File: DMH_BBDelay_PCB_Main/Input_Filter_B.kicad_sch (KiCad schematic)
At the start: 15 parts, among them U21 TL072

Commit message: Adjustments during breadboarding
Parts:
- removed C112: 4.7uF, Capacitor_THT:CP_Radial_D4.0mm_P1.50mm, symbol Device:C_Polarized
- removed R106, R243: 22k, Resistor_THT:R_Axial_DIN0207_L6.3mm_D2.5mm_P7.62mm_Horizontal, symbol Device:R_US
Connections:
- net Ref_2v5: now reaches U21.5 (+)

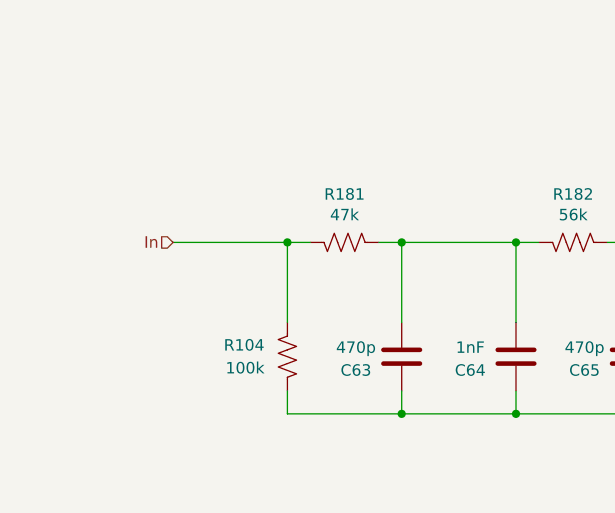
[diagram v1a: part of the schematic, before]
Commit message: More adjustments during breadboarding
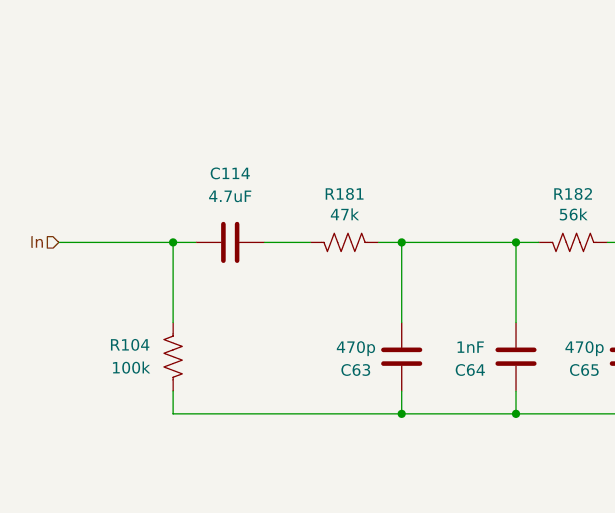
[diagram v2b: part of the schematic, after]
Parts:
- added C114: 4.7uF, Capacitor_THT:C_Disc_D4.3mm_W1.9mm_P5.00mm, symbol Device:C
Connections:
- net In: now also C114.1; no longer R181.1
- new net: C114.2, R181.1
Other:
- moved on the sheet: R104
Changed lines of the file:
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@@
+	)
+	(junction
+		(at 38.1 63.5)
+		(diameter 0)
+		(color 0 0 0 0)
 	)
 	(junction
@@
 	)
 	(junction
-		(at 50.8 63.5)
+		(at 101.6 82.55)
 		(diameter 0)
 		(color 0 0 0 0)
@@
 	)
 	(junction
-		(at 101.6 82.55)
-		(diameter 0)
-		(color 0 0 0 0)
-	)
-	(junction
 		(at 101.6 63.5)
 		(diameter 0)
@@
 	(wire
 		(pts
-			(xy 50.8 80.01) (xy 50.8 82.55)
+			(xy 38.1 80.01) (xy 38.1 82.55)
 		)
 		(stroke
@@
 	(wire
 		(pts
-			(xy 50.8 63.5) (xy 53.34 63.5)
-		)
-		(stroke
-			(width 0)
-			(type default)
-		)
-	)
-	(wire
-		(pts
 			(xy 86.36 63.5) (xy 88.9 63.5)
 		)
@@
 	(wire
 		(pts
-			(xy 50.8 82.55) (xy 63.5 82.55)
+			(xy 38.1 82.55) (xy 63.5 82.55)
 		)
 		(stroke
@@
 	(wire
 		(pts
+			(xy 38.1 63.5) (xy 40.64 63.5)
+		)
+		(stroke
+			(width 0)
+			(type default)
+		)
+	)
+	(wire
+		(pts
 			(xy 76.2 80.01) (xy 76.2 82.55)
 		)
@@
 	(wire
 		(pts
-			(xy 38.1 63.5) (xy 50.8 63.5)
+			(xy 25.4 63.5) (xy 38.1 63.5)
 		)
 		(stroke
@@
 	(wire
 		(pts
-			(xy 50.8 63.5) (xy 50.8 72.39)
+			(xy 38.1 63.5) (xy 38.1 72.39)
 		)
 		(stroke
@@
 		(pts
 			(xy 123.19 50.8) (xy 114.3 50.8)
+		)
+		(stroke
+			(width 0)
+			(type default)
+		)
+	)
+	(wire
+		(pts
+			(xy 48.26 63.5) (xy 53.34 63.5)
 		)
 		(stroke
@@
 	(hierarchical_label "In"
 		(shape input)
-		(at 38.1 63.5 180)
+		(at 25.4 63.5 180)
 		(effects
 			(font
@@
 	)
 	(symbol
+		(lib_id "Device:C")
+		(at 44.45 63.5 90)
+		(unit 1)
+		(body_style 1)
+		(exclude_from_sim no)
+		(in_bom yes)
+		(on_board yes)
+		(in_pos_files yes)
+		(dnp no)
+		(fields_autoplaced yes)
+		(property "Reference" "C114"
+			(at 44.45 55.88 90)
+			(show_name no)
+			(do_not_autoplace no)
+			(effects
+				(font
+					(size 1.27 1.27)
+				)
+			)
+		)
+		(property "Value" "4.7uF"
+			(at 44.45 58.42 90)
+			(show_name no)
+			(do_not_autoplace no)
+			(effects
+				(font
+					(size 1.27 1.27)
+				)
+			)
+		)
+		(property "Footprint" "Capacitor_THT:C_Disc_D4.3mm_W1.9mm_P5.00mm"
+			(at 48.26 62.5348 0)
+			(hide yes)
+			(show_name no)
+			(do_not_autoplace no)
+			(effects
+				(font
+					(size 1.27 1.27)
+				)
+			)
+		)
+		(property "Datasheet" ""
+			(at 44.45 63.5 0)
+			(hide yes)
+			(show_name no)
+			(do_not_autoplace no)
+			(effects
+				(font
+					(size 1.27 1.27)
+				)
+			)
+		)
+		(property "Description" "Unpolarized capacitor"
+			(at 44.45 63.5 0)
+			(hide yes)
+			(show_name no)
+			(do_not_autoplace no)
+			(effects
+				(font
+					(size 1.27 1.27)
+				)
+			)
+		)
+		(pin "1"
+		)
+		(pin "2"
+		)
+		(instances
+			(project "DMH_BBDelay_PCB_Main"
+				(path "/58f4306d-5387-4983-bb08-41a2313fd315/53120047-129a-4e0f-876f-6cafa2f18733/9104bdbd-0802-4c59-bf61-2977ca5bff15"
+					(reference "C114")
+					(unit 1)
+				)
+			)
+		)
+	)
+	(symbol
 		(lib_id "Device:R_US")
 		(at 107.95 63.5 90)
@@
 	(symbol
 		(lib_id "Device:R_US")
-		(at 50.8 76.2 0)
+		(at 38.1 76.2 0)
 		(mirror x)
 		(unit 1)
@@
 		(dnp no)
 		(property "Reference" "R104"
-			(at 48.26 74.9299 0)
+			(at 35.56 74.9299 0)
 			(show_name no)
 			(do_not_autoplace no)
@@
 		)
 		(property "Value" "100k"
-			(at 48.26 77.4699 0)
+			(at 35.56 77.4699 0)
 			(show_name no)
 			(do_not_autoplace no)
@@
 		)
 		(property "Footprint" "Resistor_THT:R_Axial_DIN0207_L6.3mm_D2.5mm_P7.62mm_Horizontal"
-			(at 51.816 75.946 90)
+			(at 39.116 75.946 90)
 			(hide yes)
 			(show_name no)
@@
 		)
 		(property "Datasheet" ""
-			(at 50.8 76.2 0)
+			(at 38.1 76.2 0)
 			(hide yes)
 			(show_name no)
@@
 		)
 		(property "Description" "Resistor, US symbol"
-			(at 50.8 76.2 0)
-			(hide yes)
-			(show_name no)
+			(at 38.1 76.2 0)
+			(hide yes)
+			(show_name no)

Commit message: Added notes from troubleshooting
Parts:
- C114: value 4.7uF -> 3.3uF
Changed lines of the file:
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@@
 			)
 		)
-		(property "Value" "4.7uF"
+		(property "Value" "3.3uF"
 			(at 44.45 58.42 90)
 			(show_name no)

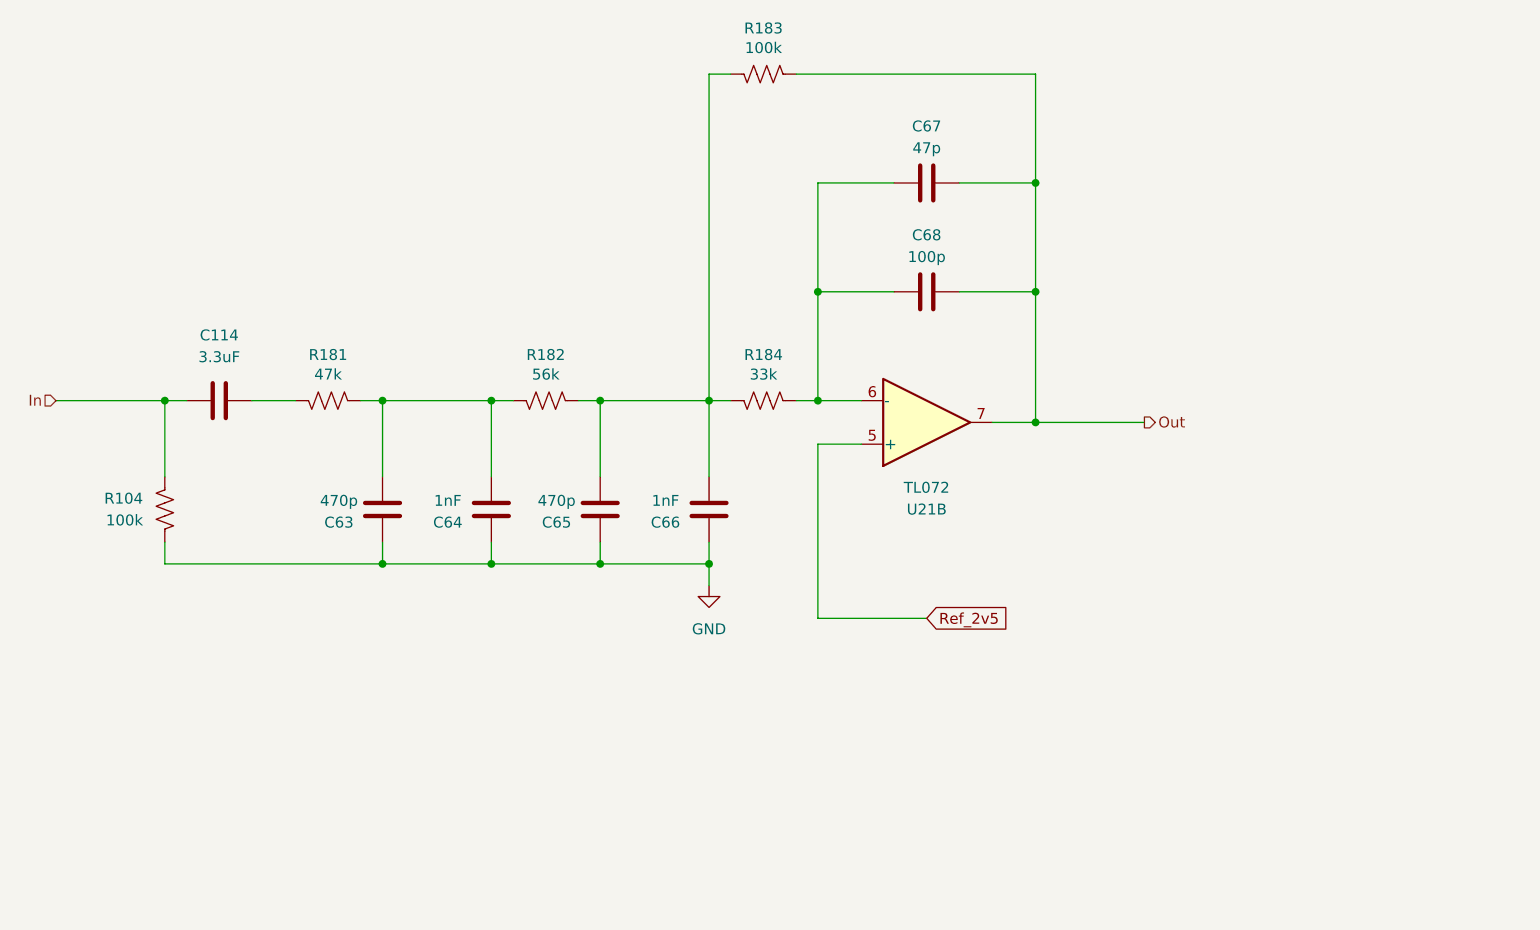
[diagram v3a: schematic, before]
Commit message: Synced channel A and B schematics
... and applied several minor improvements and optimizations.
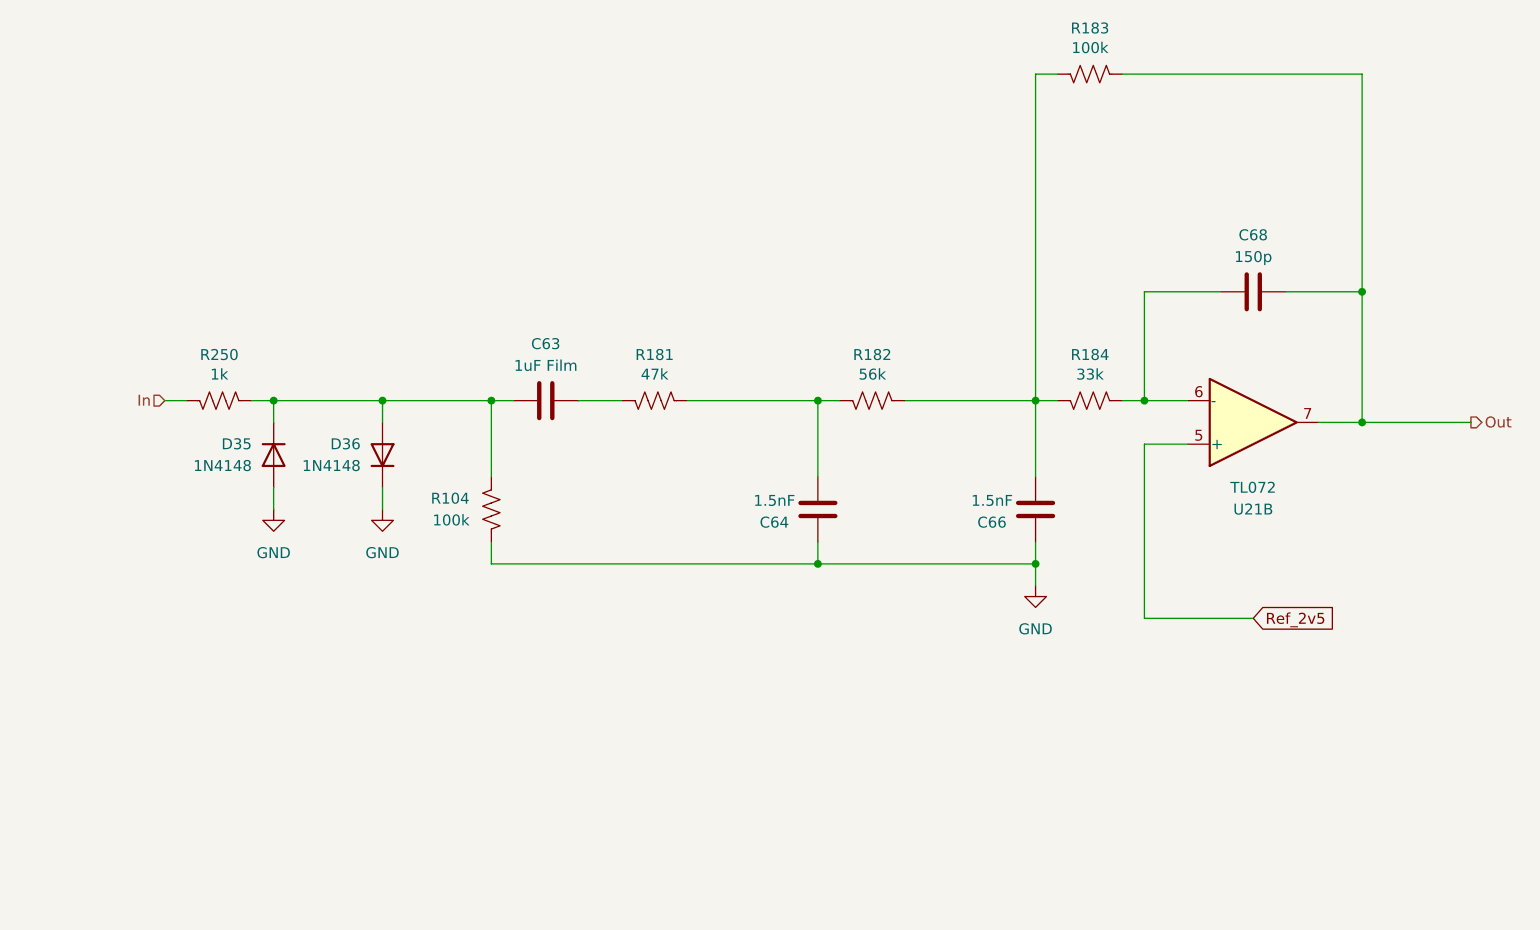
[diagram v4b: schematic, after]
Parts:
- removed C114: 3.3uF, Capacitor_THT:C_Disc_D4.3mm_W1.9mm_P5.00mm, symbol Device:C
- removed C65: 470p, Capacitor_THT:C_Disc_D3.0mm_W2.0mm_P2.50mm, symbol Device:C
- removed C67: 47p, Capacitor_THT:C_Disc_D3.0mm_W2.0mm_P2.50mm, symbol Device:C
- added D35, D36: 1N4148, Diode_THT:D_DO-35_SOD27_P7.62mm_Horizontal, symbol Diode:1N4148
- added R250: 1k, Resistor_THT:R_Axial_DIN0207_L6.3mm_D2.5mm_P7.62mm_Horizontal, symbol Device:R_US
- C63: value 470p -> 1uF Film; footprint Capacitor_THT:C_Disc_D3.0mm_W2.0mm_P2.50mm -> Capacitor_THT:C_Disc_D7.5mm_W5.0mm_P5.00mm
- C64, C66: value 1nF -> 1.5nF
- C68: value 100p -> 150p
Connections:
- net GND: now also D35.2 (A), D36.1 (K); no longer C63.1
- net In: now also R250.1; no longer R104.2
- net at C64.2, R181.2, R182.1: no longer C63.2
- net at R181.1: now also C63.2
- new net: C63.1, D35.1 (K), D36.2 (A), R104.2, R250.2
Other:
- moved on the sheet: C64, C66, C68, R104, R181, R182, R183, R184, U21B
